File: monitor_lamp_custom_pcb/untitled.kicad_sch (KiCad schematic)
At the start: 10 parts, among them J2 VEML7700_Connection, J3 LD2410C_Connection, J4 Conn_01x02, J5 SHTxx_Connection, Q3 AO3400A, U3 ESP32-C3_SUPERMINI_TH, U4 MAX40200AUK

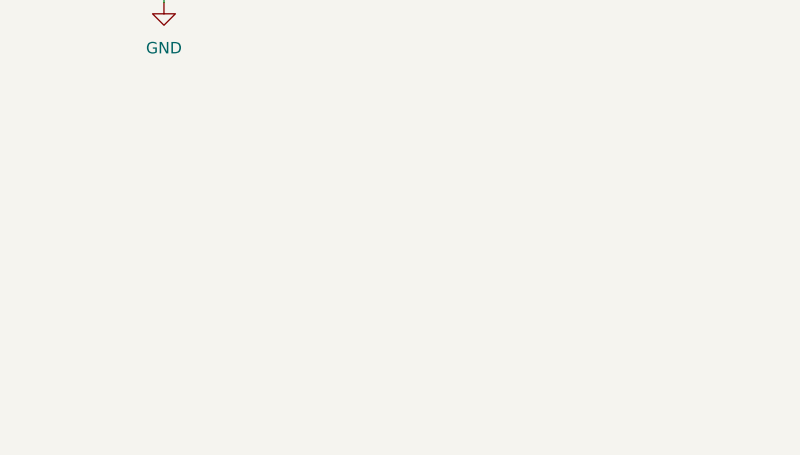
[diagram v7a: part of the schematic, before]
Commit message: Added supplementary power supply connection
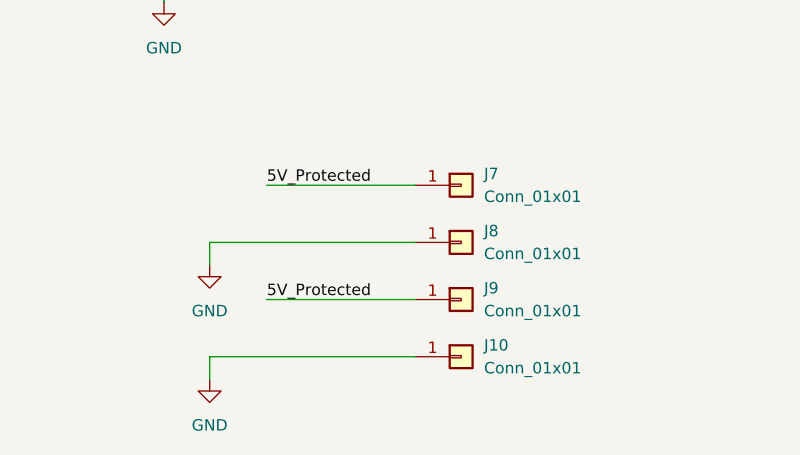
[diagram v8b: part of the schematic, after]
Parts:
- added J10, J7, J8, J9: Conn_01x01, TestPoint:TestPoint_Pad_1.0x1.0mm, symbol Connector_Generic:Conn_01x01
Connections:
- net 5V_Protected: now also J7.1 (Pin_1), J9.1 (Pin_1)
- net GND: now also J10.1 (Pin_1), J8.1 (Pin_1)
